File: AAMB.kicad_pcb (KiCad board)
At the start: 2 copper layers, 188 parts, among them J1 Screw_Terminal_01x04, J2 PJRAS4X2U01X, J3 SPKR L, J4 SPKR R, J5 Screw_Terminal_01x03, J6 Screw_Terminal_01x03, J7 Screw_Terminal_01x04, K1 G5LE-1, K2 G5LE-1, Q1 BC546, Q2 BC556, Q201 BC546, Q202 BC546, Q203 BC546, Q204 BD140, Q205 BD139, Q206 BD140, Q207 MJL21193, Q208 MJL21194, Q209 BC546, Q3 BC546, Q301 BC546, Q302 BC546, Q303 BC546, Q304 BD140, Q305 BD139, Q306 BD140, Q307 MJL21193, Q308 MJL21194, Q309 BC546, Q4 BD140, U1 TL072, U2 NE5532, U3 NE5532, U4 THAT2180, U5 DG509BEQ-T1-E3, U6 CD4071B

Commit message: Layout progress
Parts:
- C12, R12, R23, R26, R301, R302, R303, R33, R35, R44, R45, U3, U5, U6: moved to B.Cu
- R201: moved to F.Cu
- moved U6 209.8 mm to (151.1, 30.4), turned to 180 degrees
- moved U2 204.8 mm to (128.1, 19.9), turned to 180 degrees
- moved C17 202.0 mm to (126.6, 23.6)
- moved C7 201.5 mm to (136.0, 23.4), turned to 180 degrees
- moved C20 200.6 mm to (107.4, 24.3), turned to 180 degrees
- moved U5 199.2 mm to (115.4, 35.0)
- moved R18 198.6 mm to (142.6, 24.8), turned to 180 degrees
- moved C18 198.6 mm to (133.9, 18.0)
- moved C22 195.4 mm to (121.6, 27.7)
- moved R34 192.3 mm to (122.2, 22.2)
- moved R30 192.1 mm to (121.6, 26.0), turned to 180 degrees
- moved R22 191.7 mm to (133.7, 19.8), turned to 180 degrees
- moved R25 191.4 mm to (122.0, 34.2), turned to 180 degrees
- moved C19 190.2 mm to (107.1, 19.4), turned to 180 degrees
- moved C14 189.5 mm to (93.7, 33.7), turned to 180 degrees
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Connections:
- net Net-(R26-Pad2) renamed /volume/vca_in_R
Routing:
- net Net-(D3-Pad2): track 27.8 -> 0.00 mm
- net Net-(D9-Pad1): track 20.8 -> 0.00 mm
- net Net-(D1-Pad1): track 15.3 -> 0.00 mm
- net Net-(C4-Pad1): track 12.7 -> 0.00 mm
- net Net-(Q2-Pad1): track 11.6 -> 0.00 mm
- net Net-(Q2-Pad3): track 9.49 -> 0.00 mm
- net Net-(Q1-Pad1): track 8.60 -> 0.00 mm
- net Net-(C3-Pad2): track 8.04 -> 0.00 mm
- net Net-(Q2-Pad2): track 6.80 -> 0.00 mm
- net Net-(C1-Pad1): track 6.15 -> 0.00 mm
- net Net-(C2-Pad1): track 5.07 -> 0.00 mm
- net Net-(Q3-Pad1): track 2.70 -> 0.00 mm
- net Net-(C3-Pad1): track 2.69 -> 0.00 mm
- net Net-(Q3-Pad2): track 2.53 -> 0.00 mm

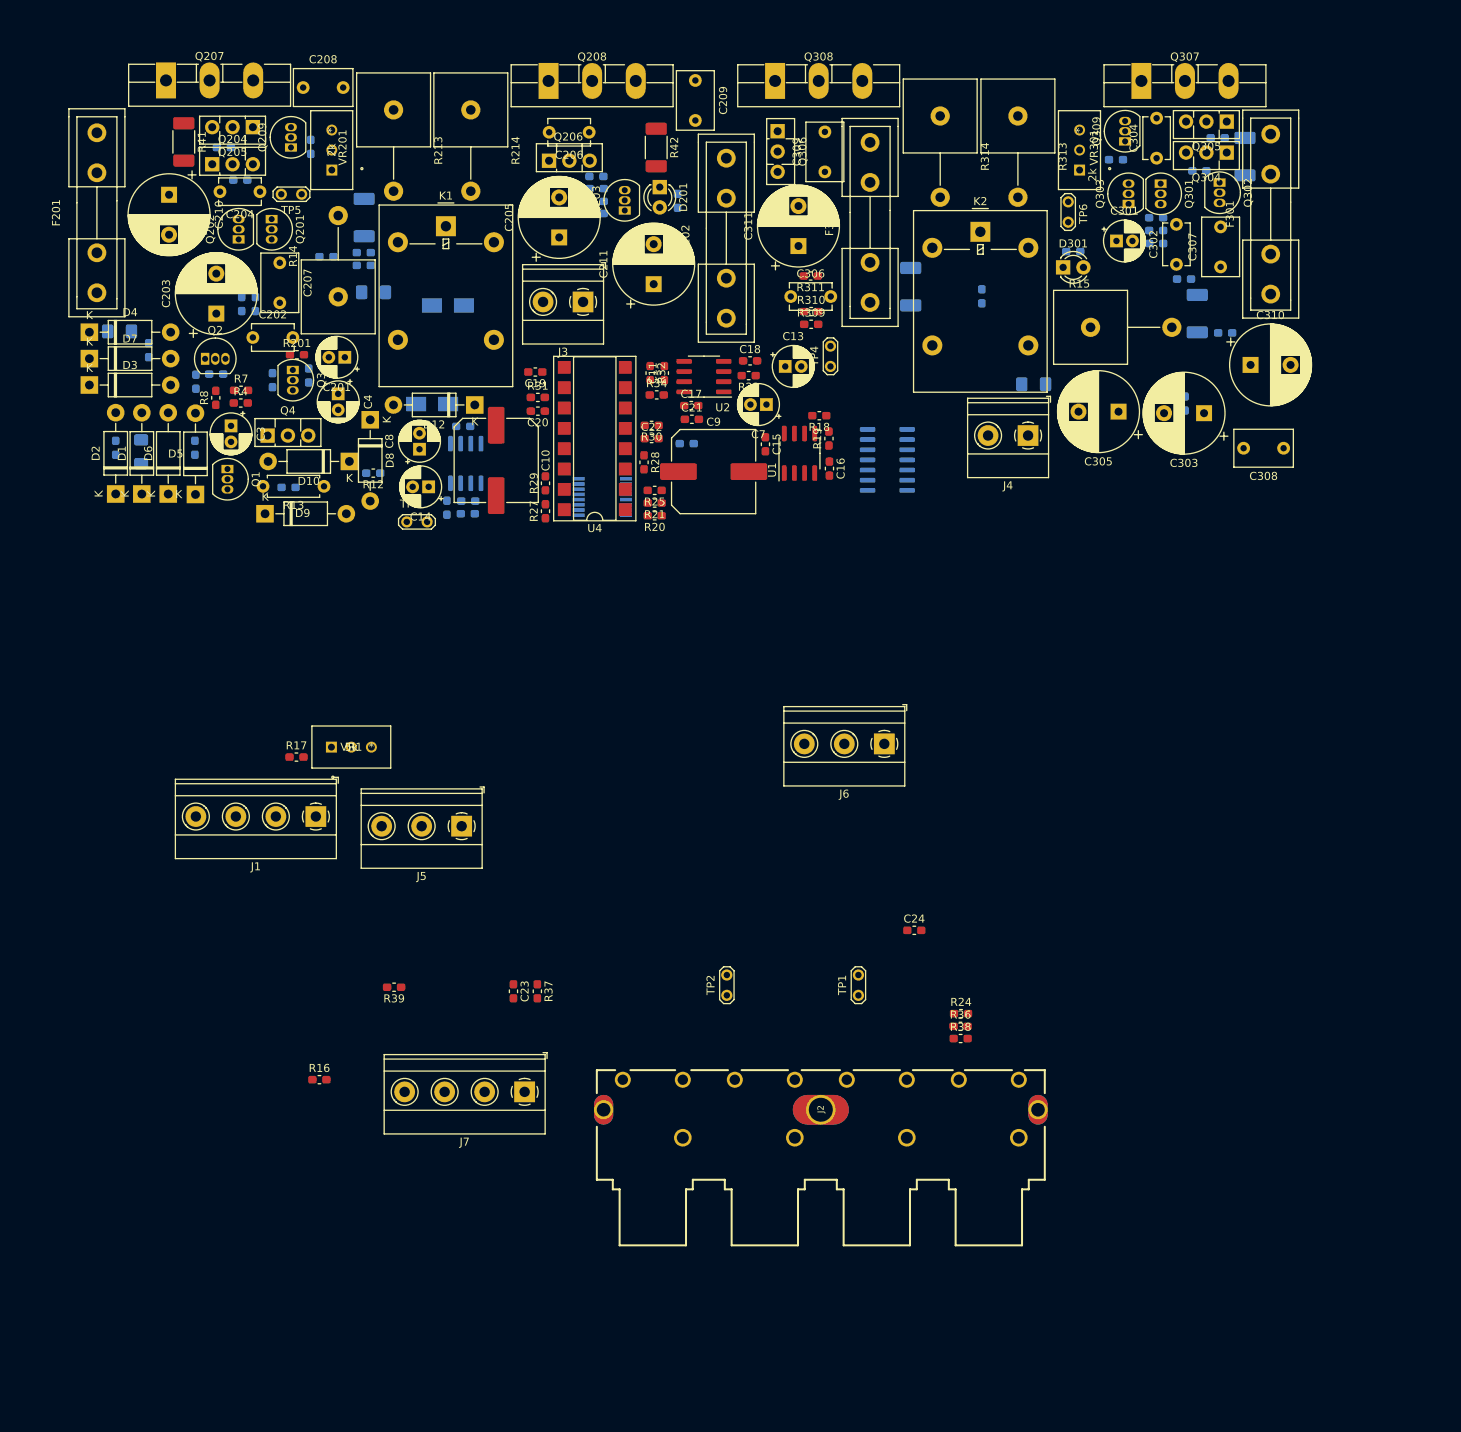
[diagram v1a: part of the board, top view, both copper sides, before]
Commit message: Just before autoroute. DRC's not addressed.
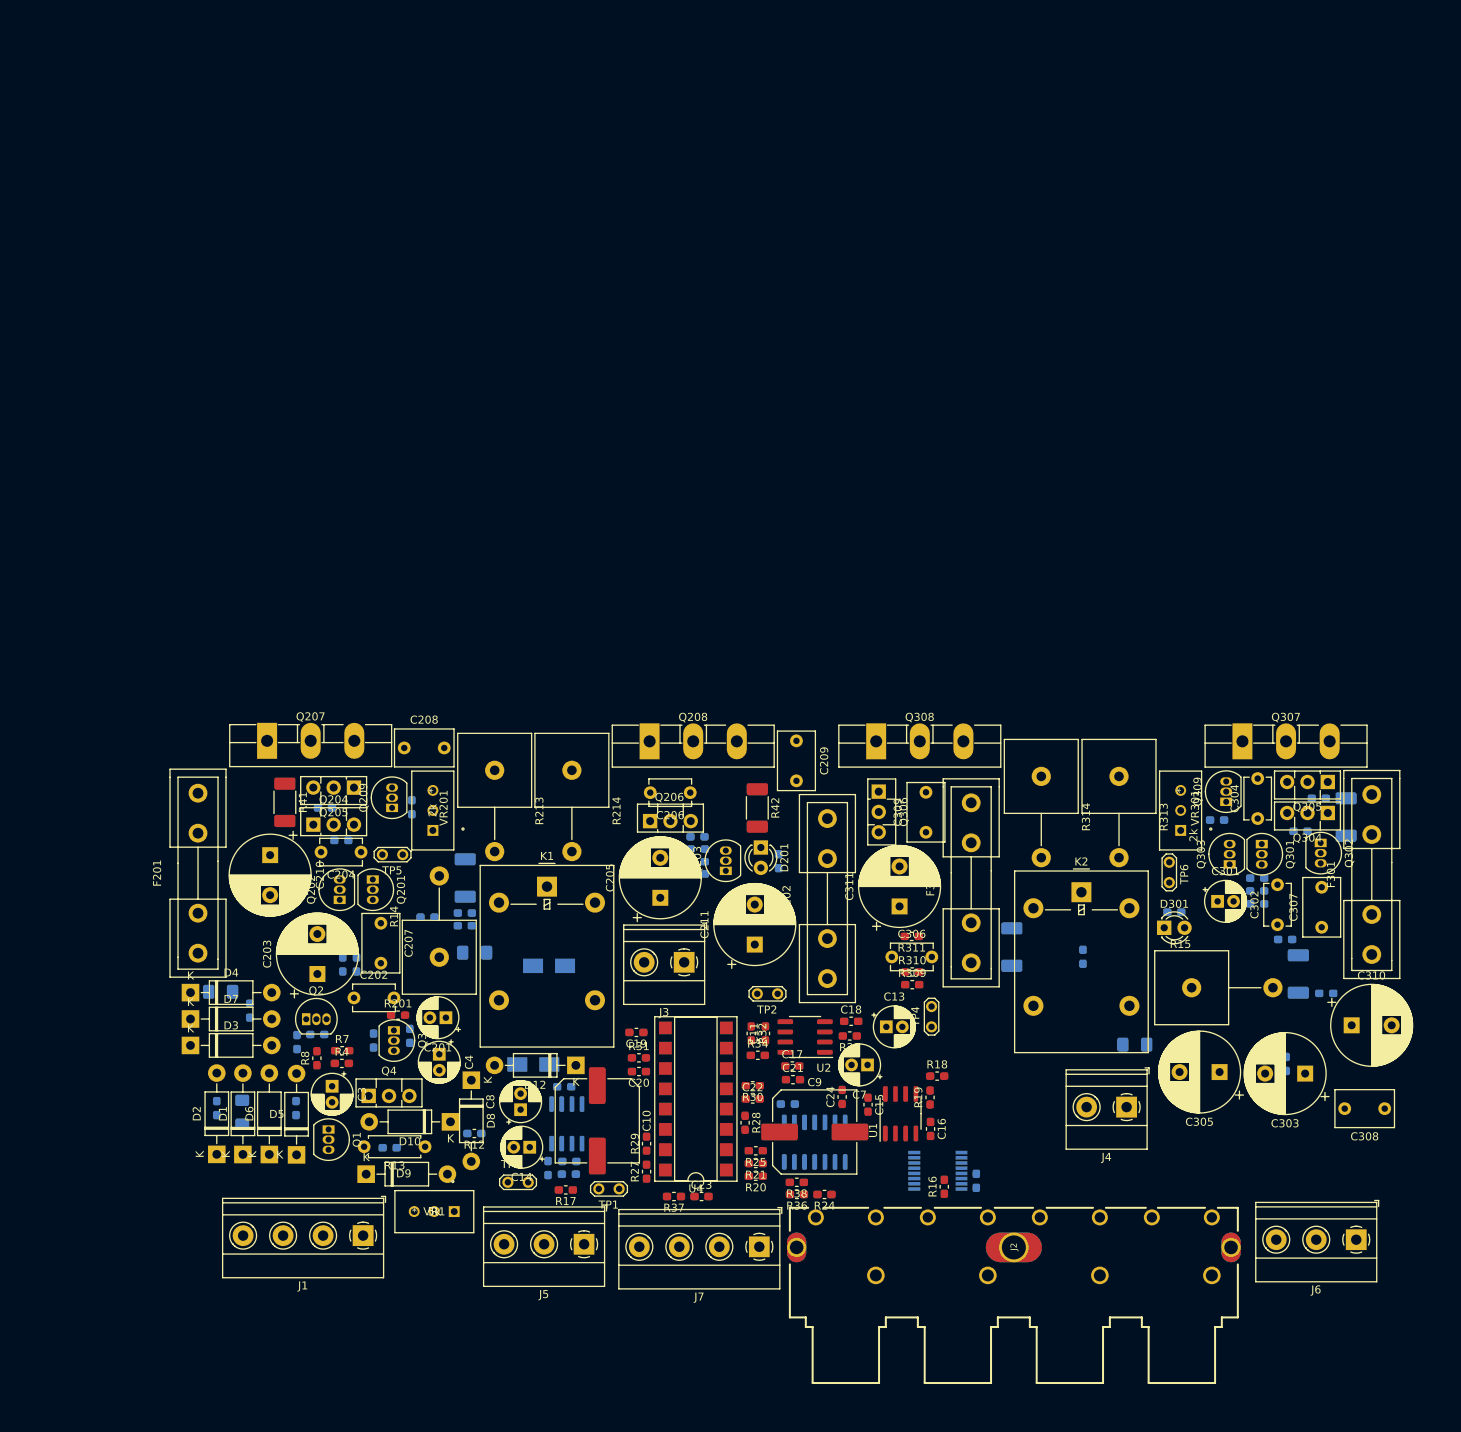
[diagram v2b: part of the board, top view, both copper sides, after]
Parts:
- R39: moved to B.Cu
- moved U5 94.1 mm to (157.4, 119.2)
- moved U6 85.8 mm to (142.0, 115.6), turned to 90 degrees
- moved J6 85.6 mm to (209.7, 127.8)
- moved J4 84.8 mm to (181.0, 111.3)
- moved R18 83.9 mm to (157.3, 107.4), turned to 0 degrees
- moved C15 83.5 mm to (148.7, 110.9)
- moved C14 83.5 mm to (106.4, 116.3)
- moved C17 83.5 mm to (139.2, 106.1)
- moved C19 83.5 mm to (119.7, 101.9)
- moved C2 83.5 mm to (67.7, 96.8)
- moved C202 83.5 mm to (84.4, 97.6)
- moved C209 83.5 mm to (139.7, 65.5)
- moved C22 83.5 mm to (134.2, 110.2)
- moved C303 83.5 mm to (203.3, 107.1)
- moved C305 83.5 mm to (192.6, 106.9)
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
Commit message: First pass auto-route
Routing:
- net +35V: track 0.00 -> 247.4 mm
- net /pwr_audio_R: track 0.00 -> 206.4 mm
- net +12V: track 0.00 -> 165.5 mm
- net -12V: track 0.00 -> 125.2 mm, vias 0 -> 1
- net -35V: track 0.00 -> 118.3 mm
- net /volume/vol_pot_3: track 0.00 -> 117.2 mm
- net /pwr_audio_L: track 0.00 -> 110.9 mm
- net /short_protection_muting/RLY_-L_+R: track 0.00 -> 94.9 mm
- net Net-(C306-Pad1): track 0.00 -> 66.5 mm
- net /pre_vol_audio_L: track 0.00 -> 57.2 mm, vias 0 -> 1
- net /volume/vol_pot_1: track 0.00 -> 55.1 mm
- net /volume/vol_pot_2: track 0.00 -> 55.0 mm
- net /audio_pwr_R/P35_fused_R: track 0.00 -> 54.5 mm
- net /audio_pwr_L/P35_fused_L: track 0.00 -> 53.8 mm
- net Net-(Q201-Pad3): track 0.00 -> 50.8 mm
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
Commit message: First pass layout. Needs DRC errors address for next pass.
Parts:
- R26, R39, U5, U6: moved to F.Cu
- moved R18 49.2 mm to (204.5, 121.0)
- moved R19 45.8 mm to (200.9, 121.0), turned to 0 degrees
- moved U1 42.8 mm to (194.9, 119.6), turned to 0 degrees
- moved C16 33.7 mm to (189.0, 122.4), turned to 0 degrees
- moved R16 23.6 mm to (181.7, 122.0)
- moved U6 19.8 mm to (161.8, 114.4), turned to 180 degrees
- moved R39 19.6 mm to (181.7, 118.7), turned to 270 degrees
- moved U5 19.4 mm to (176.7, 120.3)
- moved R26 14.9 mm to (152.8, 106.3), turned to 0 degrees
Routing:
- net /volume/vol_pot_2: track 55.0 -> 7.10 mm
- net /pwr_audio_L: track 110.9 -> 64.8 mm, vias 0 -> 1
- net Net-(R21-Pad2): track 23.9 -> 67.1 mm, vias 0 -> 2
- net Net-(R20-Pad2): track 21.1 -> 61.9 mm, vias 0 -> 2
- net /pre_vol_audio_R: track 34.1 -> 63.2 mm, vias 2 -> 1
- net -12V: track 125.2 -> 151.2 mm, vias 1 -> 4
- net /input_select/input_sw_2: track 15.2 -> 40.7 mm, vias 0 -> 2
- net /volume/vol_pot_1: track 55.1 -> 31.3 mm
- net /input_select/IN4_L: track 40.3 -> 19.2 mm
- net Net-(R24-Pad2): track 14.3 -> 35.1 mm, vias 1 -> 0
- net /audio_pwr_R/N35_low_pow_R: track 38.6 -> 59.4 mm, vias 1 -> 0
- net /input_select/IN4_R: track 26.9 -> 6.34 mm
- net Net-(R38-Pad1): track 16.8 -> 37.1 mm, vias 1 -> 0
- net /input_select/IN3_L: track 26.0 -> 6.24 mm
- net /input_select/input_sw_3: track 31.2 -> 50.3 mm, vias 0 -> 1
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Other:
- copper layers 2 -> 4

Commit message: Daily. 4-layer layout done. Only one no-connect.
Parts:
- R201: moved to B.Cu
- moved R2 104.0 mm to (166.4, 80.1), turned to 180 degrees
- moved R1 21.4 mm to (93.6, 89.3), turned to 180 degrees
- moved R3 14.0 mm to (70.2, 92.0)
- moved C24 13.6 mm to (158.9, 111.6), turned to 270 degrees
- moved R28 13.0 mm to (146.2, 111.6)
- moved C15 12.0 mm to (160.7, 111.6)
- moved C21 10.6 mm to (149.9, 108.3)
- moved R25 10.6 mm to (145.2, 117.2)
- moved C9 10.6 mm to (152.6, 114.8)
- moved R24 10.6 mm to (153.8, 122.6)
- moved R38 10.6 mm to (150.4, 121.1)
- moved C7 10.6 mm to (159.2, 106.4)
- moved R20 10.6 mm to (145.2, 120.3)
- moved R21 10.6 mm to (145.2, 118.7)
- moved R36 10.6 mm to (150.4, 122.6)
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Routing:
- net /pwr_audio_R: track 191.0 -> 54.3 mm
- net Net-(C2-Pad1): track 16.5 -> 122.7 mm, vias 0 -> 1
- net -12V: track 151.2 -> 176.0 mm, vias 4 -> 0
- net /pwr_audio_L: track 64.8 -> 40.1 mm, vias 1 -> 0
- net Net-(C1-Pad1): track 19.4 -> 42.3 mm, vias 0 -> 1
- net /volume/v_ec-: track 28.3 -> 48.9 mm
- net /audio_pwr_R/N35_fused_R: track 55.5 -> 40.2 mm
- net /input_select/input_sw_2: track 40.7 -> 52.1 mm, vias 2 -> 1
- net /short_protection_muting/RLY_-L_+R: track 79.0 -> 90.4 mm
- net Net-(R20-Pad2): track 61.9 -> 50.8 mm
- net Net-(Q2-Pad3): track 14.2 -> 25.1 mm
- net Net-(C7-Pad2): track 5.26 -> 16.1 mm
- net Net-(R24-Pad2): track 35.1 -> 24.7 mm
- net Net-(R21-Pad2): track 67.1 -> 56.7 mm
- net +12V: track 161.0 -> 150.9 mm, vias 0 -> 2
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- added copper zone on In1.Cu, net GND
- added copper zone on In2.Cu, net GND
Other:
- net class N35V added: clearance 0.4, trace_width 2, via_dia 2, via_drill 1.3
- net class P35V added: clearance 0.4, trace_width 2, via_dia 2, via_drill 1.3
- net class audio_5A removed
- net class audio_pwr_neg added: clearance 0.4, trace_width 2, via_dia 2, via_drill 1.3
- net class audio_pwr_pos added: clearance 0.4, trace_width 2, via_dia 2, via_drill 1.3

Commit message: Manual layout started.
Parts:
- moved R45 8.14 mm to (164.1, 83.5), turned to 0 degrees
- moved R307 6.66 mm to (172.2, 86.7), turned to 90 degrees
- moved Q307 4.87 mm to (200.3, 65.5)
- moved R315 2.10 mm to (202.8, 89.7)
- moved R43 2.07 mm to (203.9, 93.1), turned to 0 degrees
- moved R44 1.60 mm to (209.9, 80.9)
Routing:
- net -12V: track 176.0 -> 0.00 mm
- net +12V: track 150.9 -> 0.00 mm, vias 2 -> 0
- net Net-(C2-Pad1): track 122.7 -> 0.00 mm, vias 1 -> 0
- net /volume/vol_pot_3: track 111.5 -> 0.00 mm
- net /short_protection_muting/RLY_-L_+R: track 90.4 -> 0.00 mm
- net /pre_vol_audio_L: track 75.3 -> 0.00 mm
- net Net-(C306-Pad1): track 67.9 -> 0.00 mm, vias 1 -> 0
- net /audio_pwr_R/N35_low_pow_R: track 62.5 -> 0.00 mm
- net /input_select/input_sw_3: track 59.0 -> 0.00 mm, vias 1 -> 0
- net Net-(R21-Pad2): track 56.7 -> 0.00 mm, vias 2 -> 0
- net /pre_vol_audio_R: track 54.4 -> 0.00 mm, vias 2 -> 0
- net /input_select/input_sw_2: track 52.1 -> 0.00 mm, vias 1 -> 0
- net Net-(R20-Pad2): track 50.8 -> 0.00 mm, vias 2 -> 0
- net Net-(Q201-Pad3): track 50.8 -> 0.00 mm
- net Net-(C206-Pad1): track 49.3 -> 0.00 mm
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
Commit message: Linux test and some layout progress.
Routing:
- net Net-(C2-Pad1): track 0.00 -> 160.7 mm
- net Net-(C306-Pad1): track 0.00 -> 68.4 mm
- net Net-(C206-Pad1): track 0.00 -> 46.9 mm
- net /audio_pwr_R/N35_low_pow_R: track 0.00 -> 44.2 mm, vias 0 -> 1
- net /audio_pwr_R/pwr_fet_pos_R: track 0.00 -> 36.1 mm
- net Net-(C306-Pad2): track 0.00 -> 30.9 mm
- net Net-(Q302-Pad2): track 0.00 -> 29.1 mm
- net /audio_pwr_R/pwr_fet_neg_R: track 0.00 -> 28.9 mm
- net /audio_pwr_L/pwr_fet_pos_L: track 0.00 -> 26.9 mm
- net Net-(C304-Pad2): track 0.00 -> 17.0 mm
- net Net-(C206-Pad2): track 0.00 -> 14.5 mm
- net Net-(C1-Pad1): track 0.00 -> 14.2 mm
- net /audio_pwr_R/P35_low_pow_R: track 0.00 -> 12.8 mm
- net /audio_pwr_R/P35_fused_R: track 37.2 -> 49.3 mm
- net Net-(Q309-Pad2): track 0.00 -> 11.6 mm
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
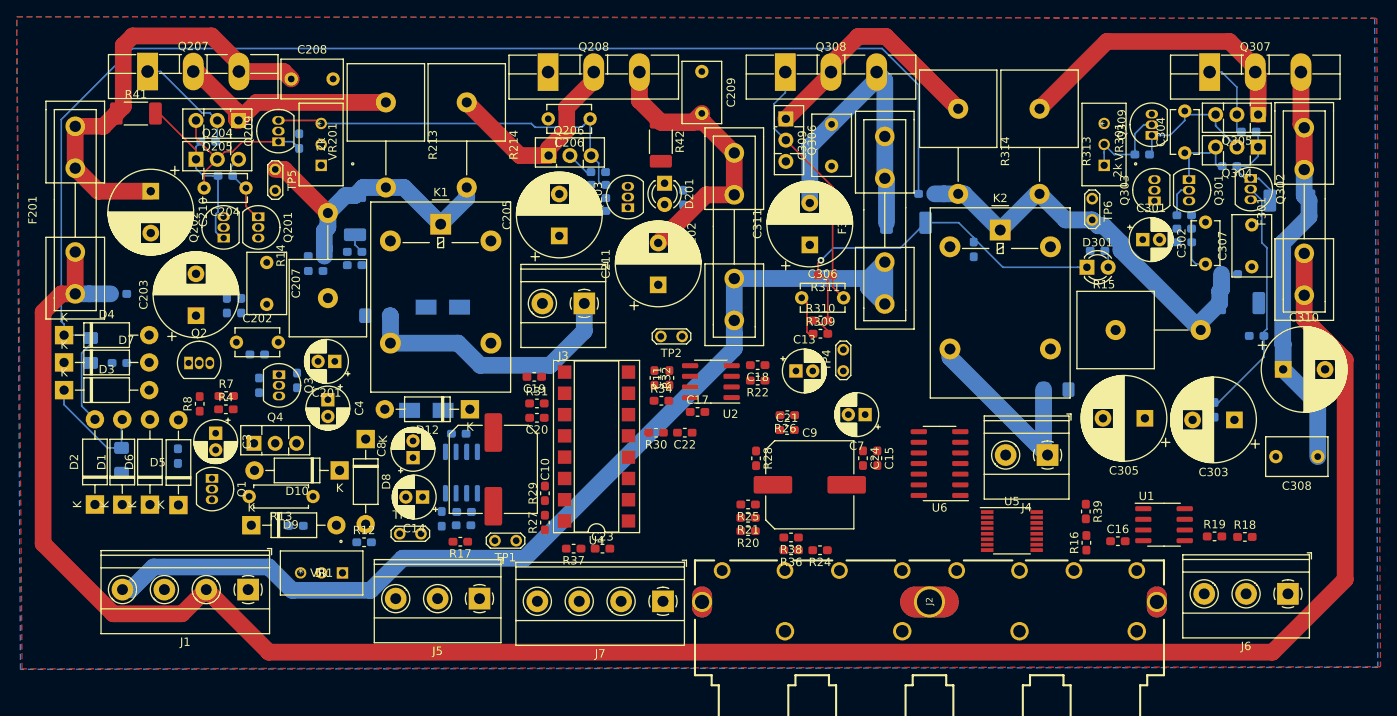
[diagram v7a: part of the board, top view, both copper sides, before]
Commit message: Routing complete. Needs silscreen cleanup and screw holes placed.
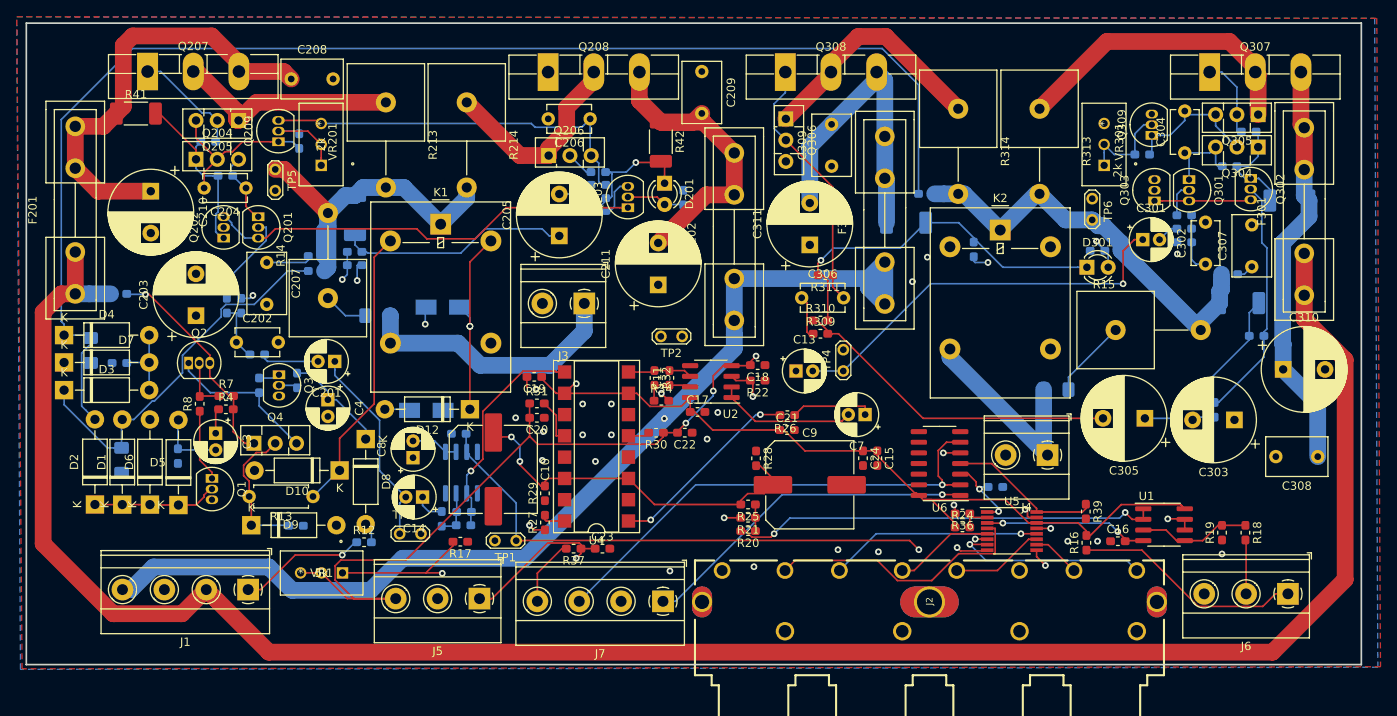
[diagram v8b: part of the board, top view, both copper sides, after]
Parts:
- R38: moved to B.Cu
- moved R38 25.1 mm to (174.8, 115.1), turned to 0 degrees
- moved R36 20.9 mm to (170.8, 118.2)
- moved R24 17.2 mm to (170.8, 119.9), turned to 0 degrees
- moved R19 0.99 mm to (201.8, 120.5), turned to 90 degrees
- moved R18 0.51 mm to (204.6, 120.5), turned to 270 degrees
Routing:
- net -12V: track 0.00 -> 148.8 mm, vias 0 -> 5
- net +12V: track 0.00 -> 135.5 mm, vias 0 -> 2
- net /volume/vol_pot_3: track 0.00 -> 112.3 mm, vias 0 -> 1
- net /short_protection_muting/RLY_-L_+R: track 0.00 -> 81.1 mm, vias 0 -> 2
- net /pre_vol_audio_L: track 0.00 -> 72.3 mm, vias 0 -> 2
- net /pre_vol_audio_R: track 0.00 -> 61.4 mm, vias 0 -> 2
- net /input_select/input_sw_3: track 0.00 -> 59.6 mm, vias 0 -> 1
- net Net-(R21-Pad2): track 0.00 -> 59.2 mm, vias 0 -> 2
- net Net-(Q201-Pad3): track 0.00 -> 51.9 mm
- net Net-(R20-Pad2): track 0.00 -> 51.2 mm, vias 0 -> 2
- net /line_audio_R: track 0.00 -> 48.2 mm, vias 0 -> 1
- net /input_select/input_sw_2: track 0.00 -> 47.8 mm, vias 0 -> 1
- net /input_select/IN1_R: track 0.00 -> 46.7 mm, vias 0 -> 1
- net /volume/v_ec-: track 0.00 -> 44.0 mm, vias 0 -> 2
- net /input_select/input_sw_1: track 0.00 -> 40.8 mm, vias 0 -> 1
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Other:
- board outline added: 159.4 x 76.6 mm
